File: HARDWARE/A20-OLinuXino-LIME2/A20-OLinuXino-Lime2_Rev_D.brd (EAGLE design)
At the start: 84 x 59.6 mm, 428 parts, among them Q1 E4SB25.000F20E15(25MHz/20pF/2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, Q3 4SB24.000F20E15/5x3.2mm/20ppm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, Q4 32768Hz/6pF, T1 BC846B, U1 A20, U10 SY6280, U11 SY6280, U12 SY6280, U13 AXP209(QFN48), U14 MCP120T475I-TT, U15 SY8008C(AA)C, U16 SY7208(SOT23-6), U17 SY8008C(AA)C, U18 FIDUCIAL, U19 FIDUCIAL, U2 K4B4G1646D-BCK0, U20 FIDUCIAL, U21 FIDUCIAL, U3 K4B4G1646D-BCK0, U4 H27UBG8T2BTR, U5 RTL8211CL-GR, U6 AT24C16BN-SH, U7 NA(RCLAMP0524P), U8 NA(RCLAMP0524P), U9 NA(RCLAMP0524P)

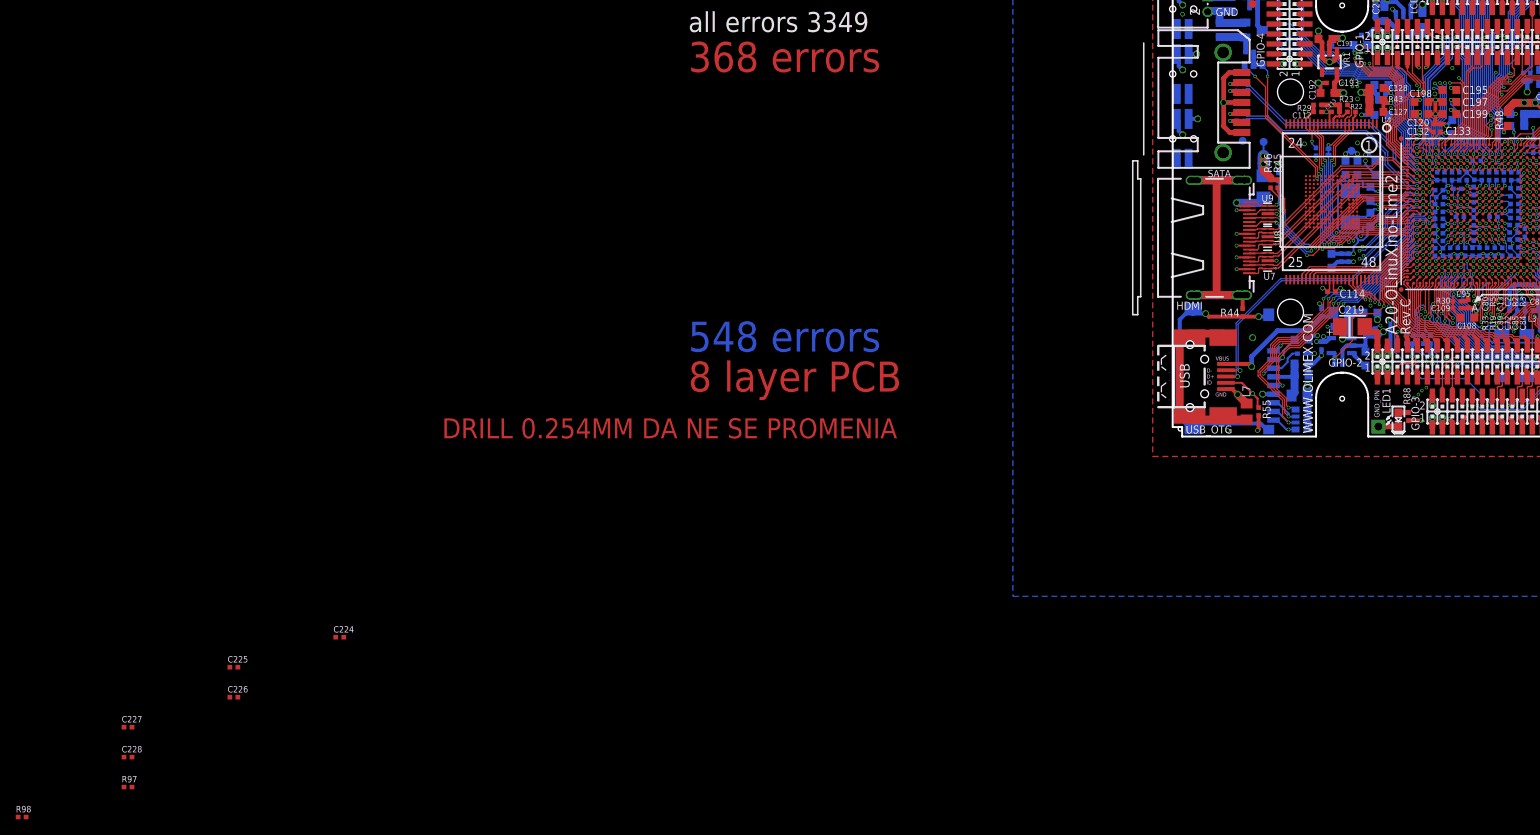
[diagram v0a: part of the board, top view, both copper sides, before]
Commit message: Re-route Sata power enable pins
With this patch, we re-route the sata power enable pins around to avoid
being in the NAND flash area, potentially freeing up space for other
purposes (eMMC) here.

This patch unfortunately has some noise in it (diff-ing eagle files is
hard)

Noise 1: Started to use eagle 7.2
Noise 2: Moved eMMC components around the PCB closer to the board
itself.

Signed-off-by: Olliver Schinagl <o.schinagl@ultimaker.com>
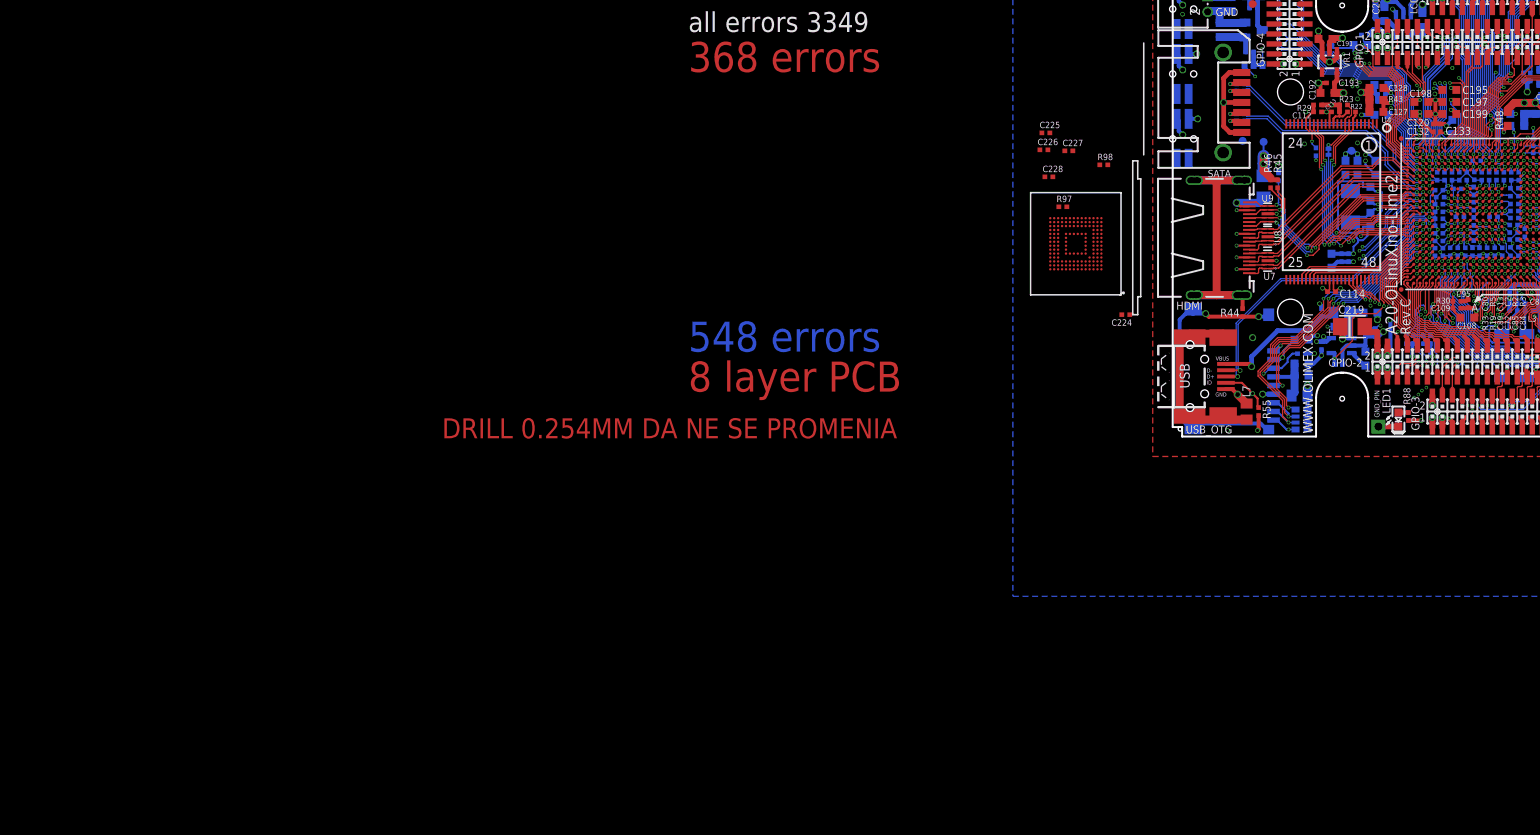
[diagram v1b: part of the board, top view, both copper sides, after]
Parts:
- moved R98 160.6 mm to (23.0, 77.9)
- moved C227 140.3 mm to (18.5, 79.6)
- moved R97 139.9 mm to (17.8, 72.5)
- moved C228 138.4 mm to (16.0, 76.3)
- moved C226 124.3 mm to (15.4, 79.8)
- moved C225 123.6 mm to (15.6, 81.9)
- moved C224 108.0 mm to (25.8, 58.8), turned to 180 degrees
- moved U$1 32.9 mm to (19.4, 67.8), turned to 180 degrees
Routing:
- net PC3/SATA-PWR-EN: track 77.3 -> 113.3 mm, vias 5 -> 3
- net PB8/SATA-PWR-EN: track 78.1 -> 85.5 mm, vias 5 -> 3
- net +5V_OTG_PWR: track 133.3 -> 136.6 mm
